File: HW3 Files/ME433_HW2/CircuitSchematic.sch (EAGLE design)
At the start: 23 parts

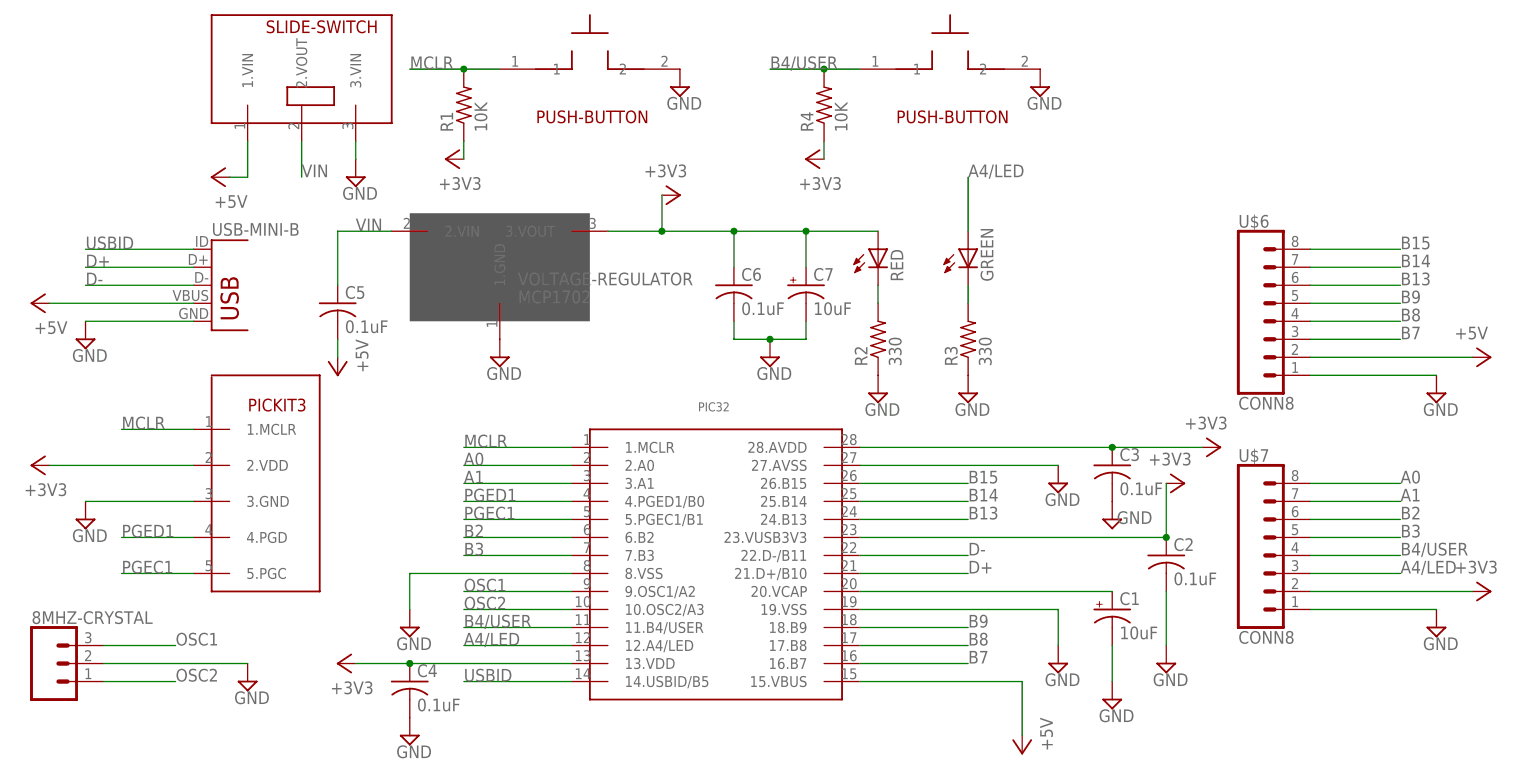
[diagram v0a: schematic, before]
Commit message: HW3 commit
- Updated folder "HW2 Files"
- Removed unnecessary project files
- Added final schematic/pcb
- Added .zip of gerber files
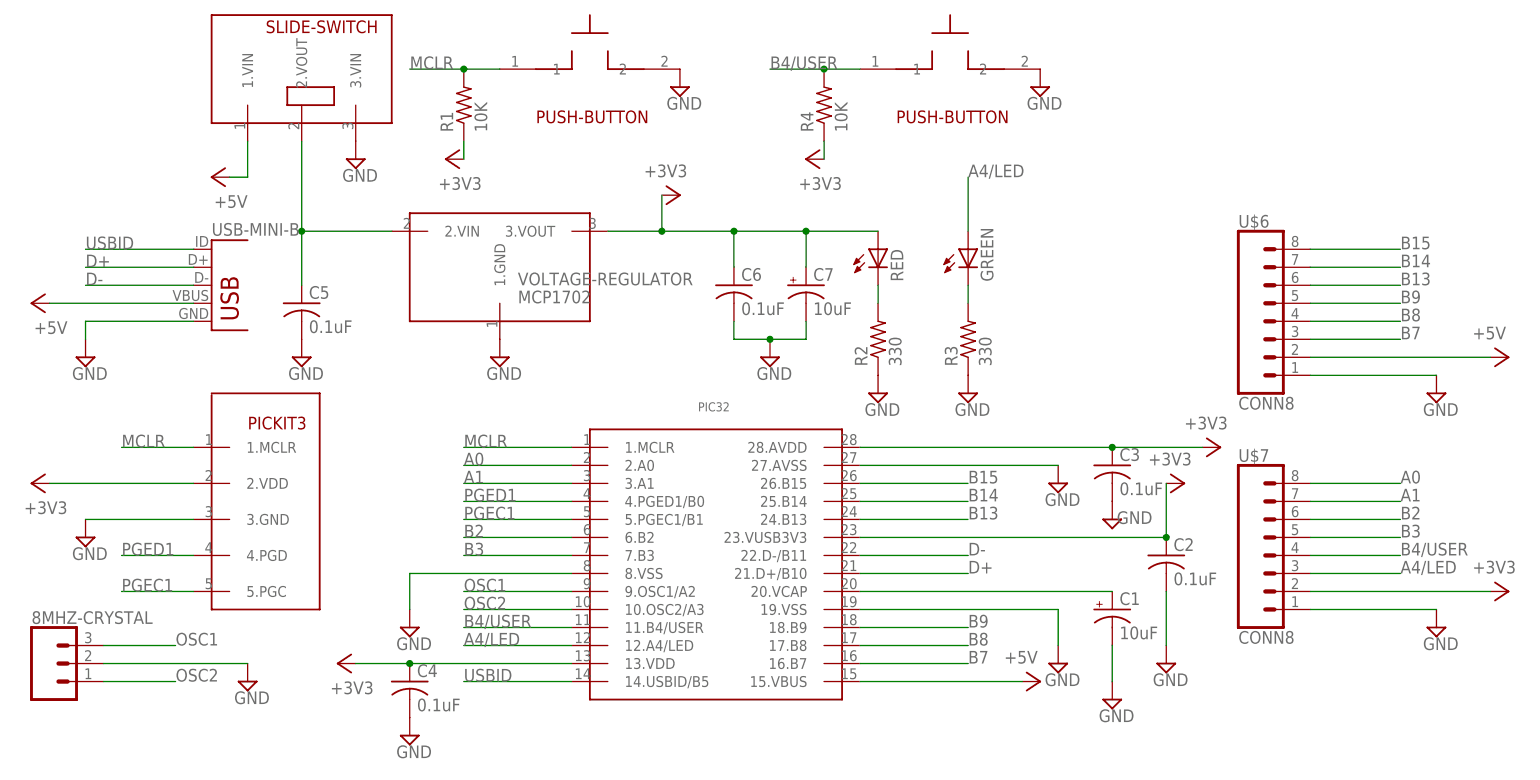
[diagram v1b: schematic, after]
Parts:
- C1, C7: device resistor:CPOL-USB45181A -> resistor:CPOL-USE5-5
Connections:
- net VIN renamed N$4
- net +5V: no longer C5.2
- net GND: now also C5.2
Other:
- moved on the sheet: C5
